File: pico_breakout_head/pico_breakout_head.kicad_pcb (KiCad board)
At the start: 2 copper layers, 39 x 66 mm, 17 parts, among them J1 HDR F 2.54MM 20-pin VERT, J2 HDR F 2.54MM 20-pin VERT, J3 JST B6B-PH-K-S, J4 HDR M 2.54MM 4p VERT, J5 JST B2B-XH-A, J6 HDR M 2.54MM 9p VERT, Q1 AS2302, U1 Pico

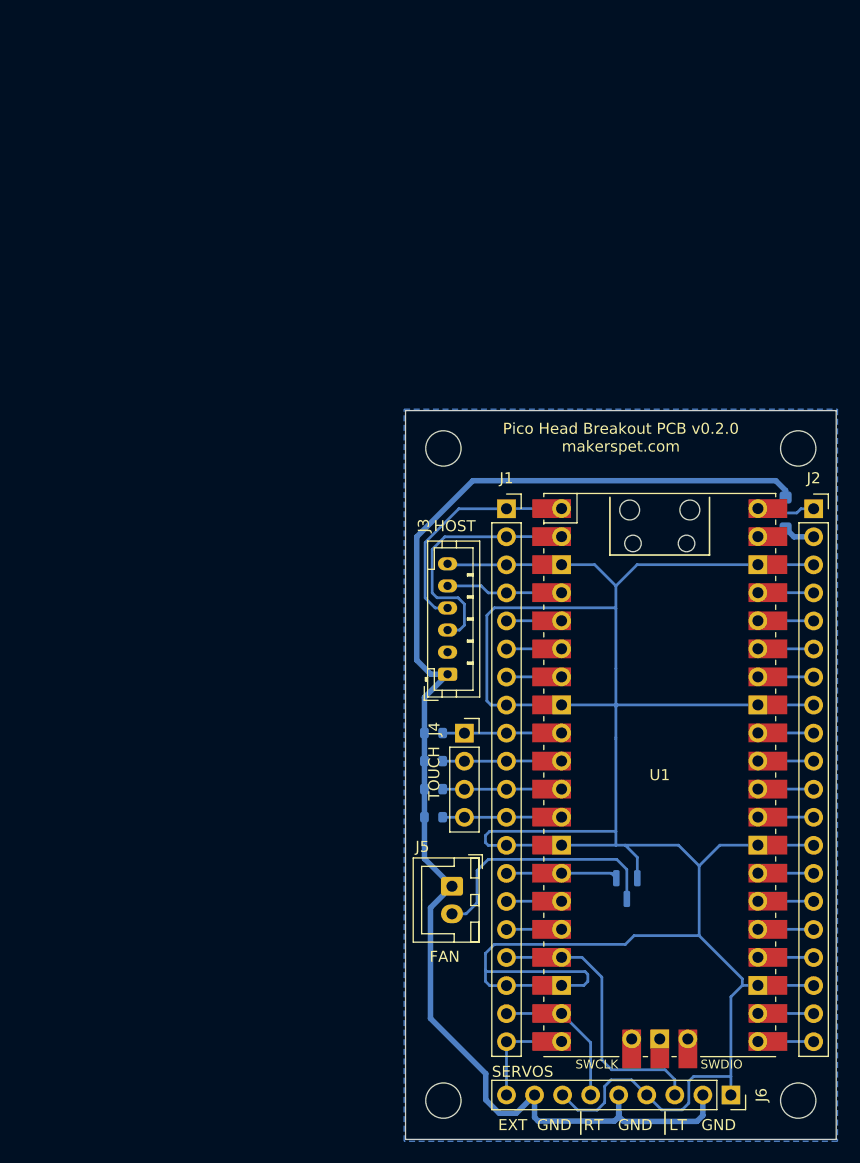
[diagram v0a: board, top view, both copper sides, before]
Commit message: ZH extension connector; 6-pin LDS connector
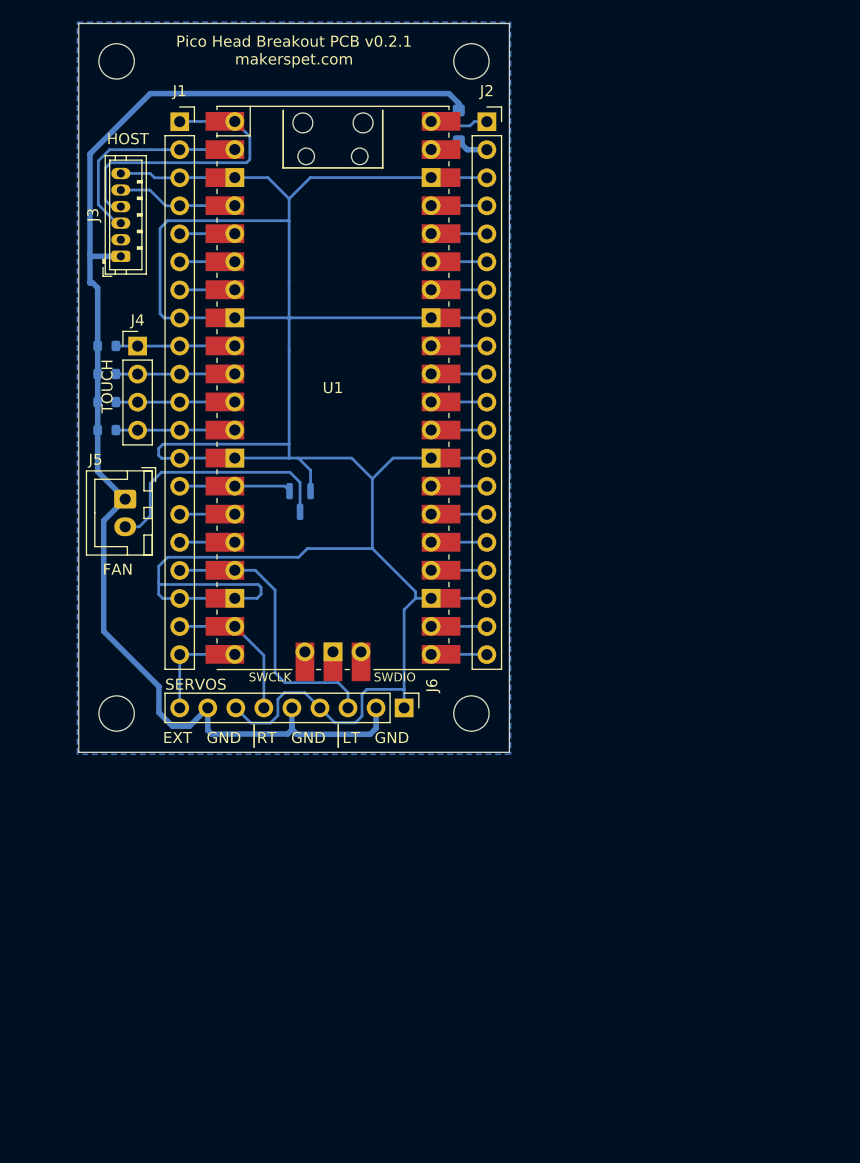
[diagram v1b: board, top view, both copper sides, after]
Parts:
- J3: value JST B6B-PH-K-S -> JST B6B-ZR; footprint Connector_JST:JST_PH_B6B-PH-K_1x06_P2.00mm_Vertical -> Makerspet:JST_ZH_B6B-ZR_1x06_P1.50mm_Vertical
- J4: value HDR M 2.54MM 4p VERT -> HDR M 2.54MM 4P VERT; footprint Connector_PinSocket_2.54mm:PinSocket_1x04_P2.54mm_Vertical -> Connector_PinHeader_2.54mm:PinHeader_1x04_P2.54mm_Vertical
- J6: value HDR M 2.54MM 9p VERT -> HDR M 2.54MM 9P VERT; footprint Connector_PinSocket_2.54mm:PinSocket_1x09_P2.54mm_Vertical -> Connector_PinHeader_2.54mm:PinHeader_1x09_P2.54mm_Vertical
- moved J3 48.0 mm to (112.5, 50.7)
- moved J6 45.9 mm to (138.2, 91.6)
- moved D2 45.9 mm to (143.1, 38.9)
- moved H2 45.9 mm to (144.3, 33.0)
- moved J1 45.9 mm to (117.9, 38.5)
- moved H1 45.9 mm to (112.1, 33.0)
- moved H4 45.9 mm to (144.3, 92.1)
- moved Q1 45.9 mm to (128.8, 72.9)
- moved R1 45.9 mm to (111.3, 58.8)
- moved R3 45.9 mm to (111.3, 63.9)
- moved H3 45.9 mm to (112.1, 92.1)
- moved J4 45.9 mm to (114.0, 58.8)
- moved J5 45.9 mm to (112.9, 72.7)
- moved R2 45.9 mm to (111.3, 61.3)
- moved R4 45.9 mm to (111.3, 66.4)
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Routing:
- net /I2C_SDA_HOST: track 21.1 -> 27.0 mm
- net /I2C_SCL_HOST: track 23.1 -> 19.5 mm
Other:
- board text added: "Pico Head Breakout PCB v0.2.1 makerspet.com"
- board text removed: "Pico Head Breakout PCB v0.2.0 makerspet.com"

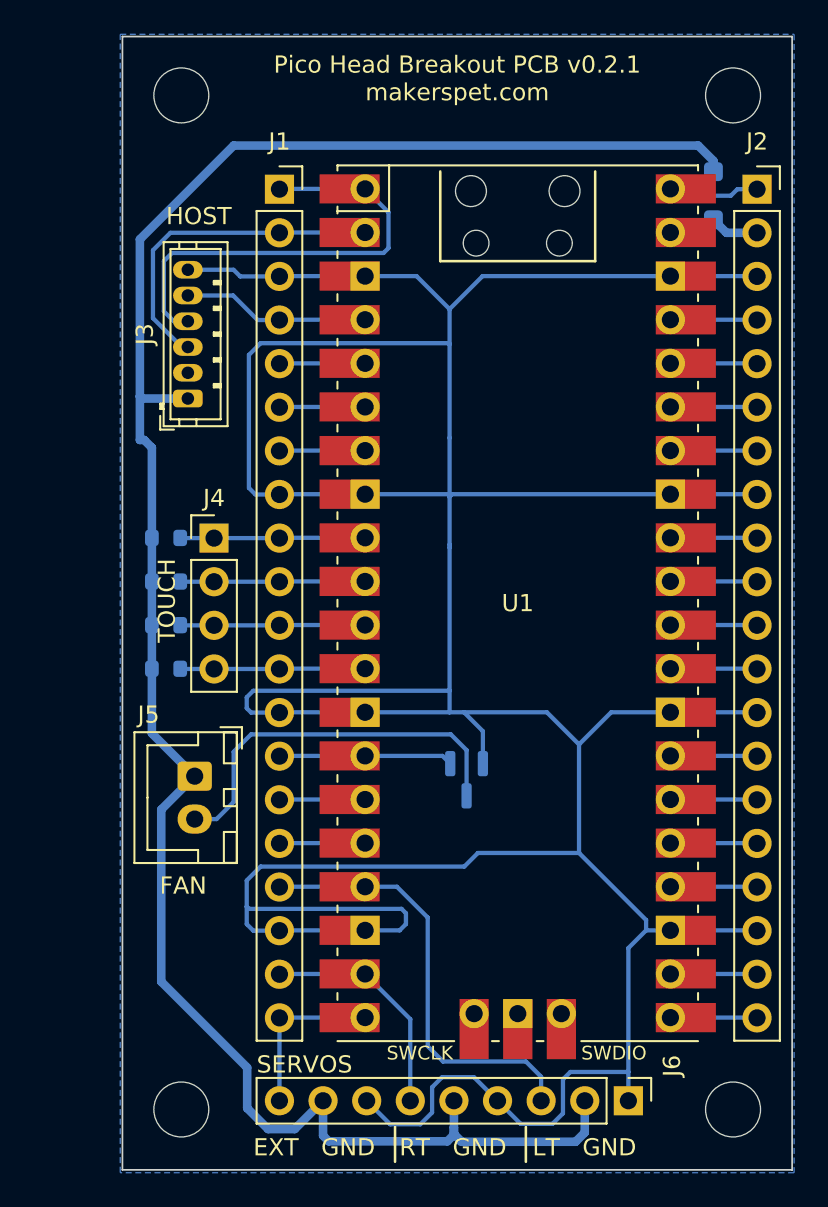
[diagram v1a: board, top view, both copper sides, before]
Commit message: Match host socket to esp32_combo
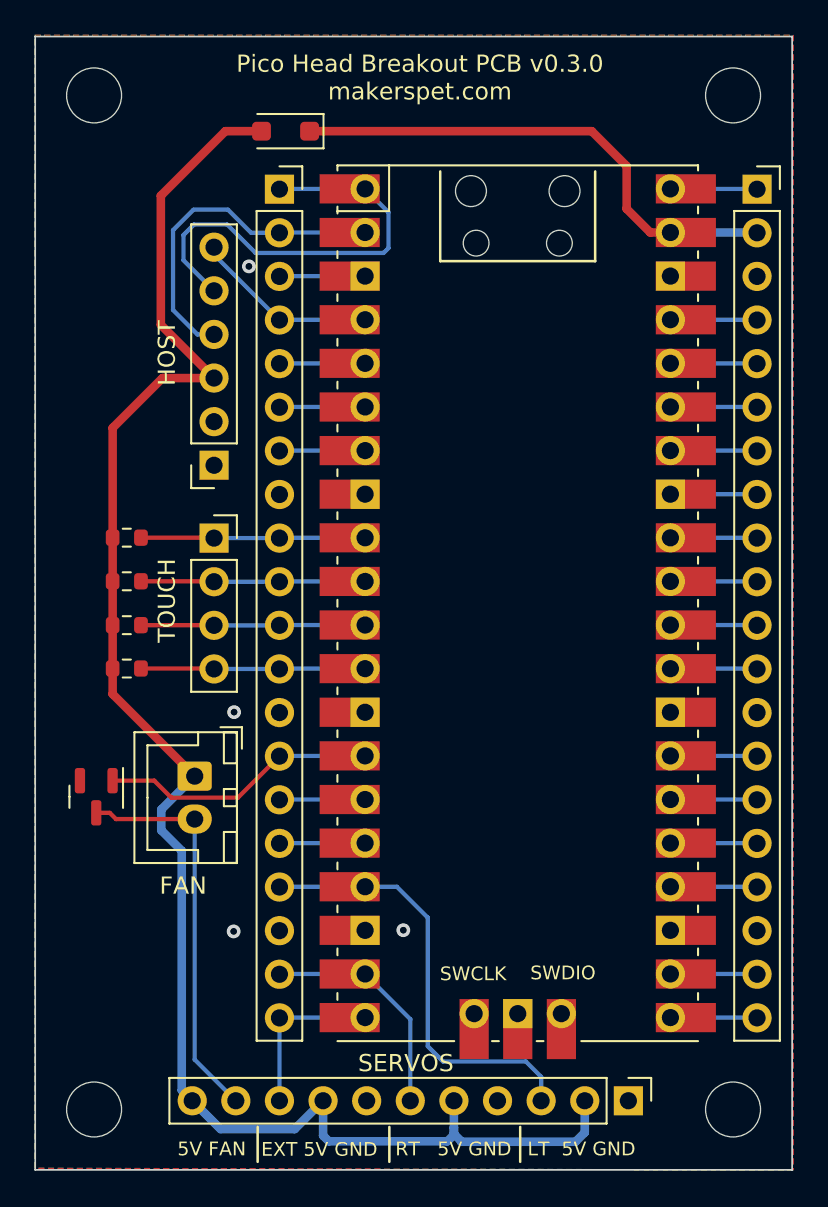
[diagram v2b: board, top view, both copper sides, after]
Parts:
- D2, Q1, R1, R2, R3, R4: moved to F.Cu
- J3: value JST B6B-ZR -> HDR SKT 2.54MM 6P VERT; footprint Makerspet:JST_ZH_B6B-ZR_1x06_P1.50mm_Vertical -> Connector_PinSocket_2.54mm:PinSocket_1x06_P2.54mm_Vertical
- J4: value HDR M 2.54MM 4P VERT -> HDR SKT 2.54MM 4P VERT; footprint Connector_PinHeader_2.54mm:PinHeader_1x04_P2.54mm_Vertical -> Connector_PinSocket_2.54mm:PinSocket_1x04_P2.54mm_Vertical
- J6: value HDR M 2.54MM 9P VERT -> HDR SKT 2.54MM 11P VERT; footprint Connector_PinHeader_2.54mm:PinHeader_1x09_P2.54mm_Vertical -> Connector_PinHeader_2.54mm:PinHeader_1x11_P2.54mm_Vertical
- moved D2 25.2 mm to (118.2, 35.1), turned to 180 degrees
- moved Q1 21.6 mm to (107.2, 73.9)
- moved H1 5.08 mm to (107.1, 33.0)
- moved H3 5.08 mm to (107.1, 92.1)
- moved J3 4.17 mm to (114.0, 54.6), turned to 180 degrees
- moved R1 2.29 mm to (109.0, 58.8)
- moved R2 2.29 mm to (109.0, 61.3)
- moved R4 2.29 mm to (109.0, 66.4)
- moved R3 2.29 mm to (109.0, 63.9)
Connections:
- J3 pad 1: +5V -> GND
- J3 pad 2: unconnected-(J3-Pin_2-Pad2) -> GND
- J3 pad 3: /I2C_SCL_HOST -> +5V
- J3 pad 4: /I2C_SDA_HOST -> /I2C_SCL_HOST
- J3 pad 5: /INT_HOST -> /I2C_SDA_HOST
- J3 pad 6: GND -> /INT_HOST
- J5 pad 2: Net-(J5-Pin_2) -> /FAN
- Q1 pad 3: Net-(J5-Pin_2) -> /FAN
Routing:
- net GND: track 248.2 -> 10.2 mm, vias 0 -> 4
- net Net-(D2-K): track 5.67 -> 30.0 mm
- net /FAN: track 0.00 -> 23.3 mm
- net Net-(J5-Pin_2): track 22.6 -> 0.00 mm
- net +5V: track 122.2 -> 100.3 mm
- net /FAN_EN: track 10.1 -> 16.1 mm
- net /TOUCH_REAR: track 10.8 -> 13.1 mm
- net /TOUCH_LEFT: track 10.8 -> 13.1 mm
- net /TOUCH_TOP: track 10.8 -> 13.1 mm
- net /TOUCH_RIGHT: track 10.8 -> 13.1 mm
- net /I2C_SDA_HOST: track 27.0 -> 26.0 mm
- added copper zone on F.Cu, net GND
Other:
- board size 39 x 66 mm -> 44.1 x 66 mm
- board text added: "5V FAN"
- board text added: "5V GND"
- board text added: "EXT 5V GND"
- board text added: "LT 5V GND"
- board text added: "Pico Head Breakout PCB v0.3.0 makerspet.com"
- board text added: "RT"
- board text removed: "EXT GND"
- board text removed: "LT GND"
- board text removed: "Pico Head Breakout PCB v0.2.1 makerspet.com"
- board text removed: "RT GND"
- board text removed: "makerspet.com"

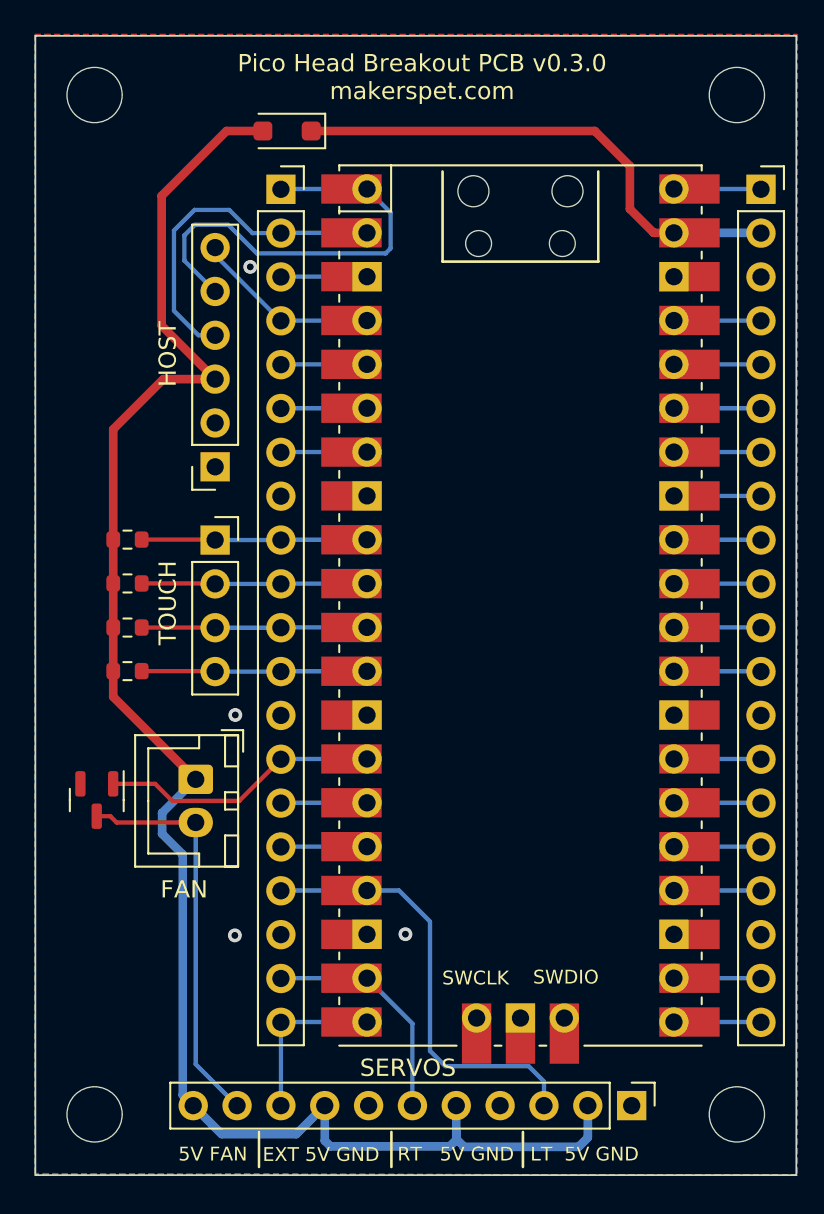
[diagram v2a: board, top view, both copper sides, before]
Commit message: esp32_combo, pico_breakout_head
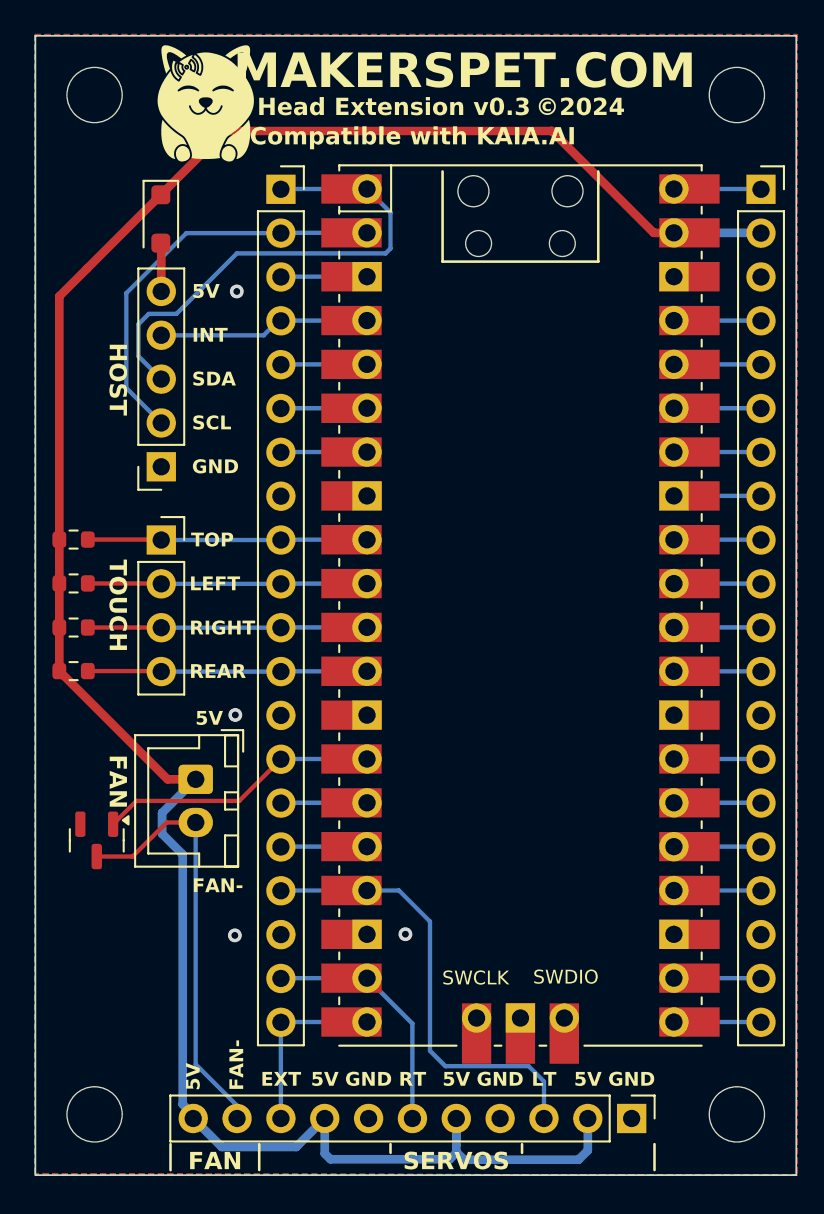
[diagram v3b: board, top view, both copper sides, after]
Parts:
- removed D2: FS26, Diode_SMD:D_SOD-123F
- added D1: FS26, Diode_SMD:D_SOD-123F, F.Cu at (110.9, 40.2)
- added G***: LOGO, Combo:Maker's Pet Logo 7mm, F.Cu at (113.5, 33.5)
- added G***: LOGO, Combo:Maker's Pet Logo 7mm, B.Cu at (131.2, 74.8)
- J3: value HDR SKT 2.54MM 6P VERT -> HDR SKT 5PIN VERT 2.54MM; footprint Connector_PinSocket_2.54mm:PinSocket_1x06_P2.54mm_Vertical -> Connector_PinSocket_2.54mm:PinSocket_1x05_P2.54mm_Vertical
- moved J3 3.12 mm to (110.9, 54.6)
- moved J4 3.12 mm to (110.9, 58.8)
- moved R1 3.12 mm to (105.8, 58.8)
- moved R2 3.12 mm to (105.8, 61.3)
- moved R3 3.12 mm to (105.8, 63.9)
- moved R4 3.12 mm to (105.8, 66.4)
- moved Q1 2.34 mm to (107.2, 76.2)
- moved J6 0.75 mm to (138.2, 92.3)
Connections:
- J2 pad 2: Net-(D2-K) -> +5V
- J3 pad 2: GND -> /I2C_SCL_HOST
- J3 pad 3: +5V -> /I2C_SDA_HOST
- J3 pad 4: /I2C_SCL_HOST -> /INT_HOST
- J3 pad 5: /I2C_SDA_HOST -> Net-(D1-A)
- U1 pad 39: Net-(D2-K) -> +5V
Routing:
- net +5V: track 100.3 -> 131.4 mm
- net Net-(D2-K): track 30.0 -> 0.00 mm
- net /I2C_SCL_HOST: track 19.9 -> 23.7 mm
- net /I2C_SDA_HOST: track 26.0 -> 29.2 mm
- net /TOUCH_RIGHT: track 13.1 -> 16.2 mm
- net /TOUCH_TOP: track 13.1 -> 16.2 mm
- net /TOUCH_REAR: track 13.1 -> 16.2 mm
- net /TOUCH_LEFT: track 13.1 -> 16.2 mm
- net Net-(D1-A): track 0.00 -> 2.81 mm
- net /INT_HOST: track 10.8 -> 12.3 mm
- net /FAN: track 23.3 -> 24.5 mm
- net /SERVO_RIGHT: track 13.5 -> 14.0 mm
- net /SERVO_EXT: track 9.82 -> 10.4 mm
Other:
- board text added: "5V"
- board text added: "Compatible with KAIA.AI"
- board text added: "EXT"
- board text added: "FAN-"
- board text added: "GND"
- board text added: "Head Extension v0.3"
- board text added: "INT"
- board text added: "LEFT"
- board text added: "LT"
- board text added: "MAKERSPET.COM"
- board text added: "REAR"
- board text added: "RIGHT"
- board text added: "SCL"
- board text added: "SDA"
- board text added: "TOP"
- board text added: "©2024"
- board text removed: "5V FAN"
- board text removed: "5V GND"
- board text removed: "EXT 5V GND"
- board text removed: "LT 5V GND"
- board text removed: "Pico Head Breakout PCB v0.3.0 makerspet.com"
